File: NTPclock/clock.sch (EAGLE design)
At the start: 23 parts, among them IC1 MAX7219CNG

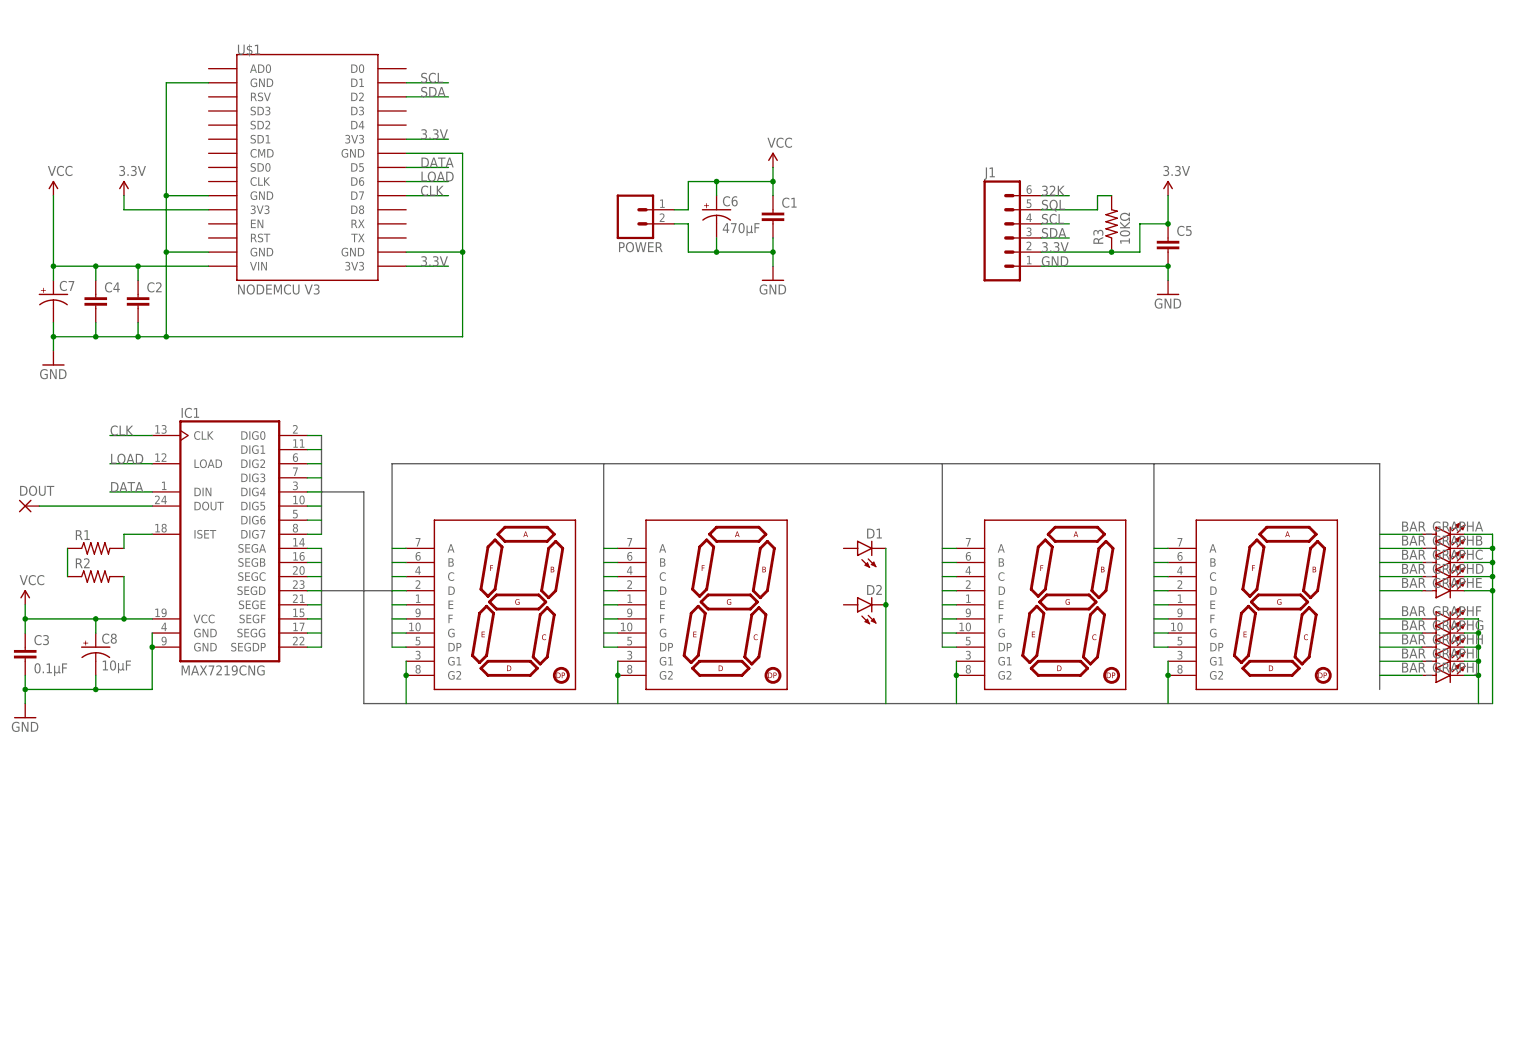
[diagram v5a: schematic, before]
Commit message: added buzzer, finished routing ground plane
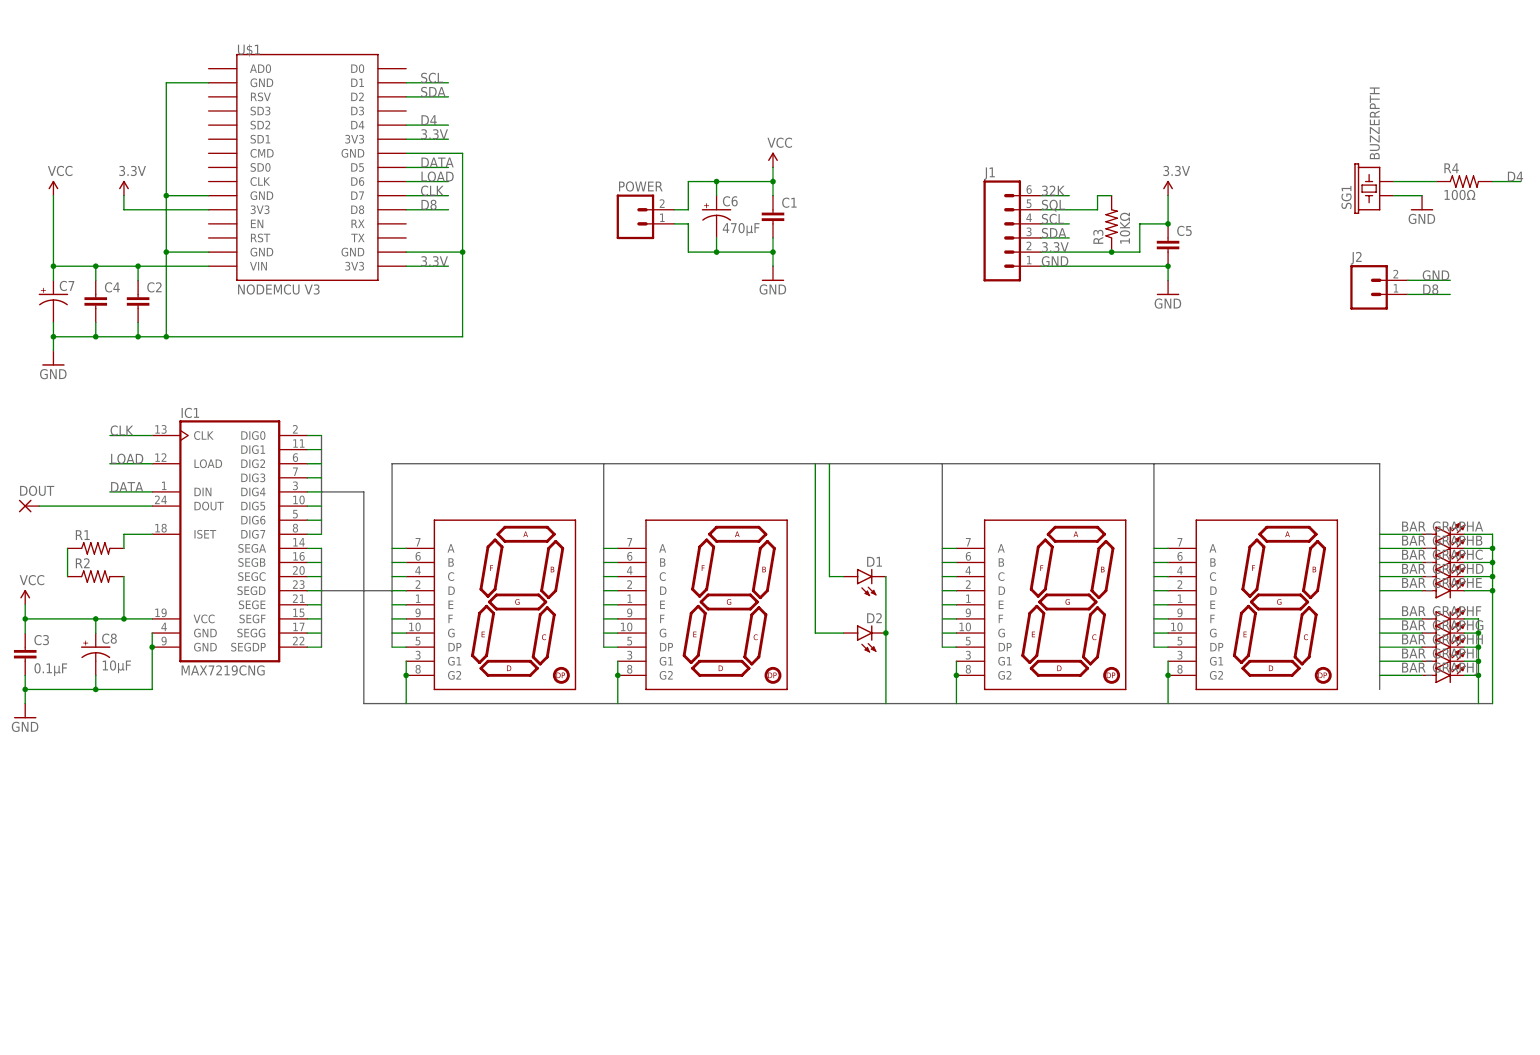
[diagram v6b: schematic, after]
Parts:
- added J2: (no value), SparkFun-Connectors:M02PTH
- added R4: 100Ω, SparkFun-Resistors:RESISTOR1206
- added SG1: BUZZERPTH, SparkFun-Electromechanical:BUZZERPTH
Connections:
- new net D4: R4.2, U$1.D4
- new net D8: J2.1, U$1.D8
- new net N$8: R4.1, SG1.2
- net D: now also D2.A
- net F: now also D1.A
- net GND: now also J2.2, POWER.1, SG1.1; no longer POWER.2
- net VCC: now also POWER.2; no longer POWER.1
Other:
- moved on the sheet: D1, D2, POWER
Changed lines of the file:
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@@
 <part name="D1" library="SparkFun-LED" deviceset="LED" device="3MM"/>
 <part name="D2" library="SparkFun-LED" deviceset="LED" device="3MM"/>
+<part name="SG1" library="SparkFun-Electromechanical" deviceset="BUZZER" device="PTH"/>
+<part name="J2" library="SparkFun-Connectors" deviceset="M02" device="PTH"/>
+<part name="R4" library="SparkFun-Resistors" deviceset="RESISTOR" device="1206" value="100Ω"/>
+<part name="GND5" library="SparkFun-Aesthetics" deviceset="GND" device=""/>
 </parts>
 <sheets>
@@
 <instance part="C7" gate="G$1" x="10.16" y="83.82"/>
 <instance part="C8" gate="G$1" x="17.78" y="20.32"/>
-<instance part="POWER" gate="G$1" x="114.3" y="99.06" rot="MR180"/>
+<instance part="POWER" gate="G$1" x="114.3" y="96.52"/>
 <instance part="J1" gate="G$1" x="182.88" y="93.98"/>
 <instance part="DIG_3" gate="G$1" x="231.14" y="27.94"/>
@@
 <instance part="GND1" gate="1" x="210.82" y="83.82"/>
 <instance part="SUPPLY2" gate="G$1" x="22.86" y="101.6"/>
-<instance part="D1" gate="G$1" x="154.94" y="38.1" rot="R90"/>
-<instance part="D2" gate="G$1" x="154.94" y="27.94" rot="R90"/>
+<instance part="D1" gate="G$1" x="154.94" y="33.02" rot="R90"/>
+<instance part="D2" gate="G$1" x="154.94" y="22.86" rot="R90"/>
+<instance part="SG1" gate="G$1" x="248.92" y="101.6" rot="R90"/>
+<instance part="J2" gate="G$1" x="246.38" y="83.82"/>
+<instance part="R4" gate="G$1" x="264.16" y="104.14"/>
+<instance part="GND5" gate="1" x="256.54" y="99.06"/>
 </instances>
 <busses>
@@
 </segment>
 <segment>
-<pinref part="POWER" gate="G$1" pin="2"/>
+<pinref part="POWER" gate="G$1" pin="1"/>
 <wire x1="121.92" y1="96.52" x2="124.46" y2="96.52" width="0.1524" layer="91"/>
 <pinref part="C1" gate="G$1" pin="2"/>
@@
 <wire x1="27.94" y1="12.7" x2="27.94" y2="20.32" width="0.1524" layer="91"/>
 <junction x="17.78" y="12.7"/>
+</segment>
+<segment>
+<pinref part="J2" gate="G$1" pin="2"/>
+<wire x1="254" y1="86.36" x2="261.62" y2="86.36" width="0.1524" layer="91"/>
+<label x="256.54" y="86.36" size="1.778" layer="95"/>
+</segment>
+<segment>
+<pinref part="SG1" gate="G$1" pin="1"/>
+<wire x1="251.46" y1="101.6" x2="256.54" y2="101.6" width="0.1524" layer="91"/>
+<pinref part="GND5" gate="1" pin="GND"/>
 </segment>
 </net>
@@
 <wire x1="248.92" y1="15.24" x2="256.54" y2="15.24" width="0.1524" layer="91"/>
 </segment>
+<segment>
+<wire x1="147.32" y1="53.34" x2="147.32" y2="22.86" width="0.1524" layer="91"/>
+<pinref part="D2" gate="G$1" pin="A"/>
+<wire x1="147.32" y1="22.86" x2="152.4" y2="22.86" width="0.1524" layer="91"/>
+</segment>
 </net>
 <net name="E" class="0">
@@
 <pinref part="IC1" gate="G$1" pin="SEGF"/>
 <wire x1="58.42" y1="25.4" x2="55.88" y2="25.4" width="0.1524" layer="91"/>
+</segment>
+<segment>
+<wire x1="149.86" y1="53.34" x2="149.86" y2="33.02" width="0.1524" layer="91"/>
+<pinref part="D1" gate="G$1" pin="A"/>
+<wire x1="149.86" y1="33.02" x2="152.4" y2="33.02" width="0.1524" layer="91"/>
 </segment>
 </net>
@@
 <segment>
 <pinref part="D2" gate="G$1" pin="C"/>
-<wire x1="160.02" y1="10.16" x2="160.02" y2="27.94" width="0.1524" layer="91"/>
+<wire x1="160.02" y1="10.16" x2="160.02" y2="22.86" width="0.1524" layer="91"/>
 <pinref part="D1" gate="G$1" pin="C"/>
-<wire x1="160.02" y1="27.94" x2="160.02" y2="38.1" width="0.1524" layer="91"/>
-<junction x="160.02" y="27.94"/>
+<wire x1="160.02" y1="22.86" x2="160.02" y2="33.02" width="0.1524" layer="91"/>
+<junction x="160.02" y="22.86"/>
 </segment>
 </net>
@@
 <net name="VCC" class="0">
 <segment>
-<pinref part="POWER" gate="G$1" pin="1"/>
+<pinref part="POWER" gate="G$1" pin="2"/>
 <wire x1="121.92" y1="99.06" x2="124.46" y2="99.06" width="0.1524" layer="91"/>
 <wire x1="124.46" y1="99.06" x2="124.46" y2="104.14" width="0.1524" layer="91"/>
@@
 </segment>
 </net>
+<net name="D4" class="0">
+<segment>
+<pinref part="U$1" gate="G$1" pin="D4"/>
+<wire x1="73.66" y1="114.3" x2="81.28" y2="114.3" width="0.1524" layer="91"/>
+<label x="76.2" y="114.3" size="1.778" layer="95"/>
+</segment>
+<segment>
+<pinref part="R4" gate="G$1" pin="2"/>
+<wire x1="269.24" y1="104.14" x2="274.32" y2="104.14" width="0.1524" layer="91"/>
+<label x="271.78" y="104.14" size="1.778" layer="95"/>
+</segment>
+</net>
+<net name="D8" class="0">
+<segment>
+<pinref part="U$1" gate="G$1" pin="D8"/>
+<wire x1="73.66" y1="99.06" x2="81.28" y2="99.06" width="0.1524" layer="91"/>
+<label x="76.2" y="99.06" size="1.778" layer="95"/>
+</segment>
+<segment>
+<pinref part="J2" gate="G$1" pin="1"/>
+<wire x1="254" y1="83.82" x2="261.62" y2="83.82" width="0.1524" layer="91"/>
+<label x="256.54" y="83.82" size="1.778" layer="95"/>
+</segment>
+</net>
+<net name="N$8" class="0">
+<segment>
+<pinref part="R4" gate="G$1" pin="1"/>
+<pinref part="SG1" gate="G$1" pin="2"/>
+<wire x1="259.08" y1="104.14" x2="251.46" y2="104.14" width="0.1524" layer="91"/>
+</segment>
+</net>

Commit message: Correct size of LEDs.  Also reroute entire LED area.
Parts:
- DIG_0, DIG_1, DIG_2, DIG_3: value 7-SEGMENT-DISPLAY-1"-RED -> 7-SEGMENT-DISPLAY-REAL-1"; device SparkFun-Displays:7-SEGMENT-DISPLAY-1"-RED -> custom_display:7-SEGMENT-DISPLAY-REAL-1"
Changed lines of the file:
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@@
 <part name="POWER" library="SparkFun-Connectors" deviceset="M02" device="JST-PTH-VERT"/>
 <part name="J1" library="SparkFun-Connectors" deviceset="M06" device="POLAR"/>
-<part name="DIG_3" library="SparkFun-Displays" deviceset="7-SEGMENT-DISPLAY-1&quot;-RED" device=""/>
-<part name="DIG_2" library="SparkFun-Displays" deviceset="7-SEGMENT-DISPLAY-1&quot;-RED" device=""/>
-<part name="DIG_1" library="SparkFun-Displays" deviceset="7-SEGMENT-DISPLAY-1&quot;-RED" device=""/>
-<part name="DIG_0" library="SparkFun-Displays" deviceset="7-SEGMENT-DISPLAY-1&quot;-RED" device=""/>
+<part name="DIG_3" library="custom_display" deviceset="7-SEGMENT-DISPLAY-REAL-1&quot;" device=""/>
+<part name="DIG_2" library="custom_display" deviceset="7-SEGMENT-DISPLAY-REAL-1&quot;" device=""/>
+<part name="DIG_1" library="custom_display" deviceset="7-SEGMENT-DISPLAY-REAL-1&quot;" device=""/>
+<part name="DIG_0" library="custom_display" deviceset="7-SEGMENT-DISPLAY-REAL-1&quot;" device=""/>
 <part name="BAR_GRAPH" library="SparkFun-LED" deviceset="LED_BARGRAPH_10" device=""/>
 <part name="DOUT" library="wirepad" deviceset="1,6/0,9" device=""/>

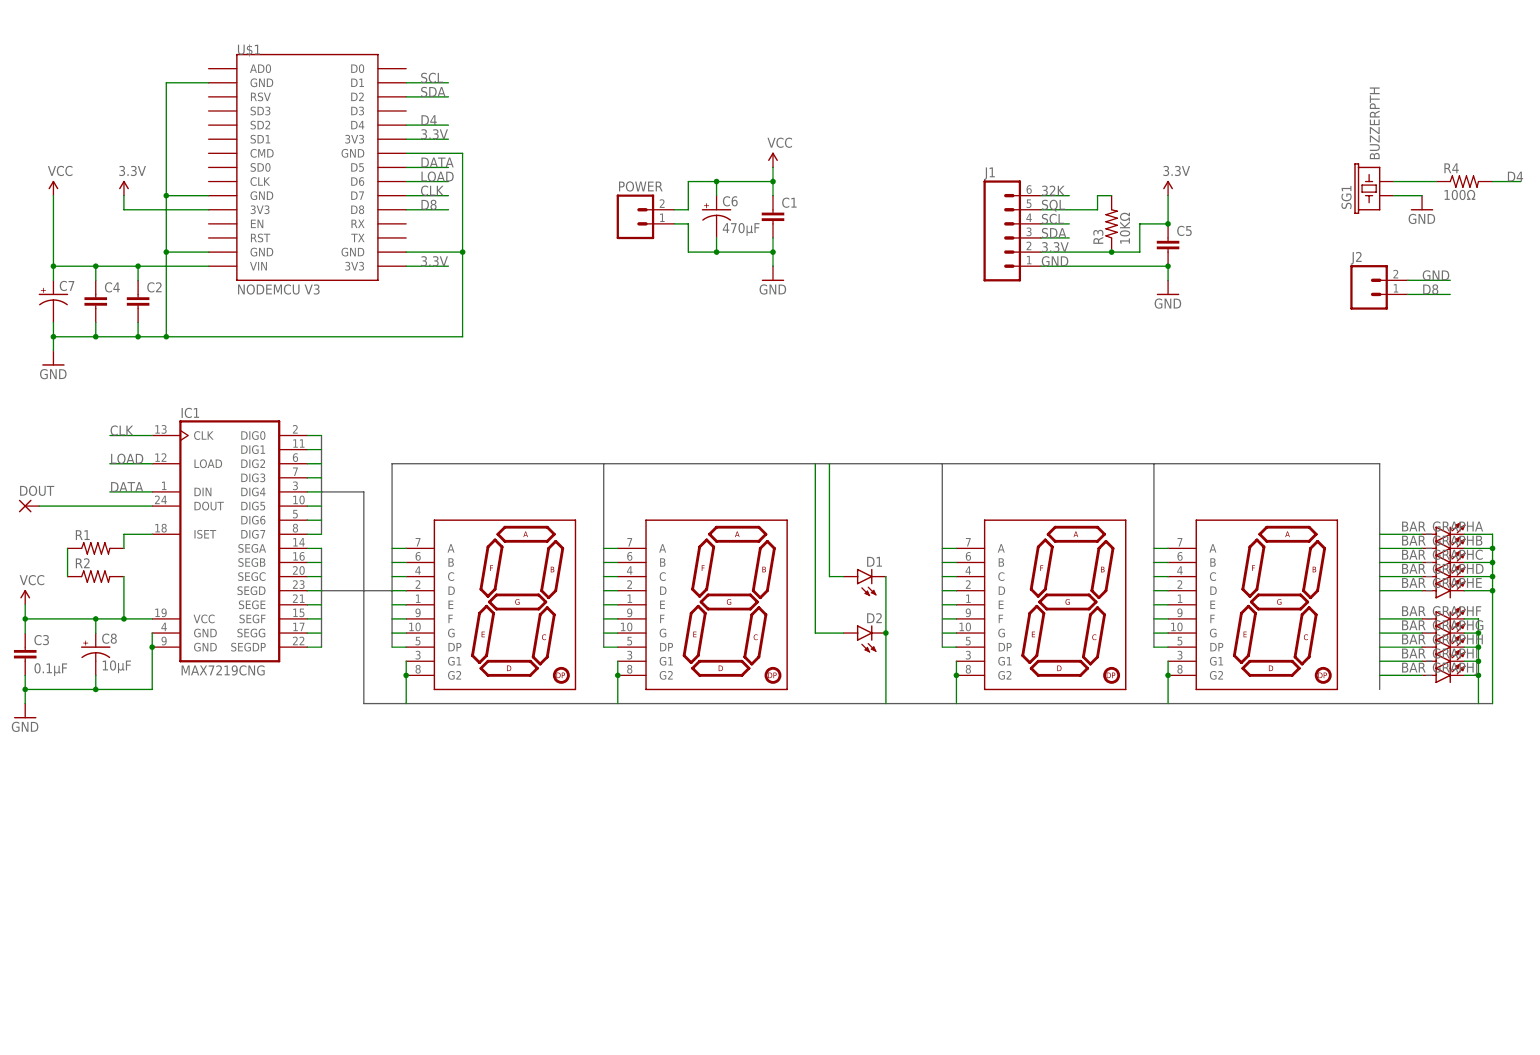
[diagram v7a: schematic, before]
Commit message: Re-organize Schematic.  Add license.
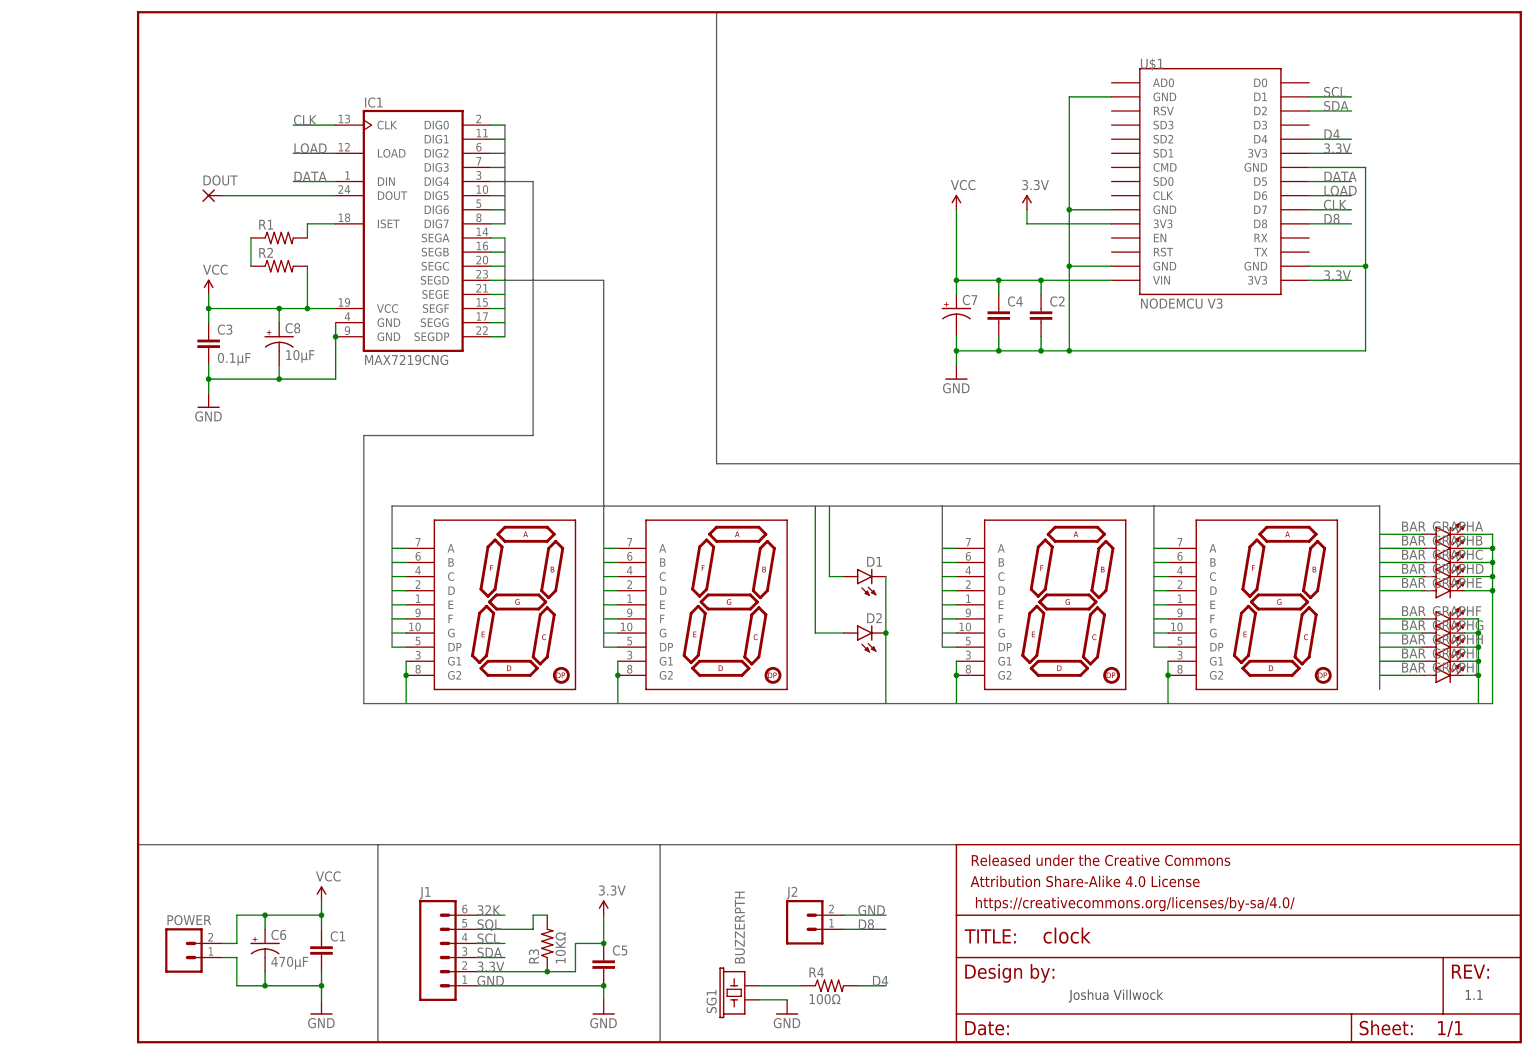
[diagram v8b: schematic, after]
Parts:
- added FRAME1: FRAME-LETTER, SparkFun-Aesthetics:FRAME-LETTER
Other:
- note added: "1.1"
- note added: "Joshua Villwock"
- moved on the sheet: C1, C2, C3, C4, C5, C6, C7, C8, DOUT, IC1, J1, J2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
